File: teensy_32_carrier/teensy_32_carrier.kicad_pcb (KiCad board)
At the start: 4 copper layers, 65 x 56.5 mm, 65 parts, among them J1 CON_01X03_PTH_2.54MM, J10 CJ, J11 CJ, J12 CJ, J13 CJ, J14 CJ, J2 CON_01X08_PTH_2.54MM, J3 CON_01X06_PTH_2.54MM, J4 CON_01X04_PTH_2.54MM, J5 CON_01X03_PTH_2.54MM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

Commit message: start routing
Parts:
- moved D1 41.5 mm to (137.0, 68.5), turned to 0 degrees
- moved R4 37.8 mm to (136.5, 69.5), turned to 0 degrees
- moved R5 37.8 mm to (136.5, 68.0), turned to 0 degrees
- moved R3 34.0 mm to (133.0, 70.0), turned to 0 degrees
- moved R8 14.6 mm to (95.5, 108.5), turned to 270 degrees
- moved R12 2.24 mm to (84.0, 82.5)
- moved R11 2.22 mm to (81.5, 82.5)
- moved C6 1.50 mm to (93.0, 86.5)
- moved R9 1.12 mm to (105.5, 109.5), turned to 270 degrees
- moved R16 0.74 mm to (97.5, 96.0)
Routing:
- net GND: track 0.00 -> 145.1 mm, vias 0 -> 6
- net +5V: track 0.00 -> 65.5 mm, vias 0 -> 4
- net /Power/OFF_NODE: track 0.00 -> 29.6 mm, vias 0 -> 3
- net /Power/BAT_IN: track 0.00 -> 25.3 mm, vias 0 -> 1
- net /Power/VR_FB: track 0.00 -> 25.1 mm, vias 0 -> 2
- net +BATT: track 0.00 -> 21.9 mm, vias 0 -> 1
- net /Power/VR_SW: track 0.00 -> 18.1 mm, vias 0 -> 1
- net /Power/VR_BT: track 0.00 -> 16.7 mm, vias 0 -> 2
- net /Power/VR_VI: track 0.00 -> 14.8 mm, vias 0 -> 1
- net /Power/VR_EN: track 0.00 -> 6.13 mm, vias 0 -> 1
- net /Power/VR_SS: track 0.00 -> 5.48 mm, vias 0 -> 1
- net Net-(D1-Pad4): track 0.00 -> 4.01 mm, vias 0 -> 1
- net Net-(D1-Pad3): track 0.00 -> 3.14 mm, vias 0 -> 1
- net Net-(D1-Pad2): track 0.00 -> 3.10 mm, vias 0 -> 1
- net /Power/VR_RT: track 0.00 -> 2.19 mm, vias 0 -> 1
- added copper zone on B.Cu, net +5V
- added copper zone on F.Cu, net +5V
- added copper zone on F.Cu, net +BATT
- added copper zone on F.Cu, net /Power/BAT_IN
- added copper zone on F.Cu, net /Power/VR_SW
- added copper zone on B.Cu, net GND
- added copper zone on F.Cu, net GND

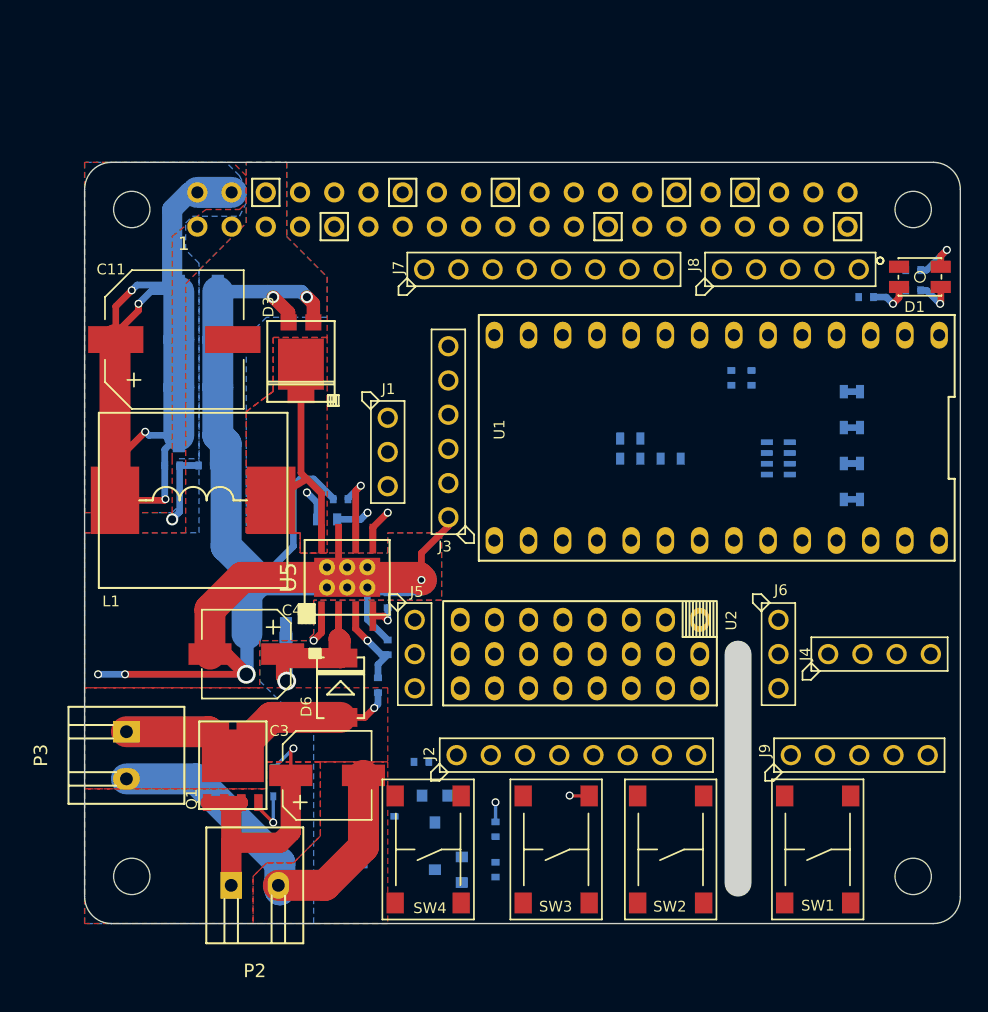
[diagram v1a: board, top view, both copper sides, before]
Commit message: routing getting closer to first completion
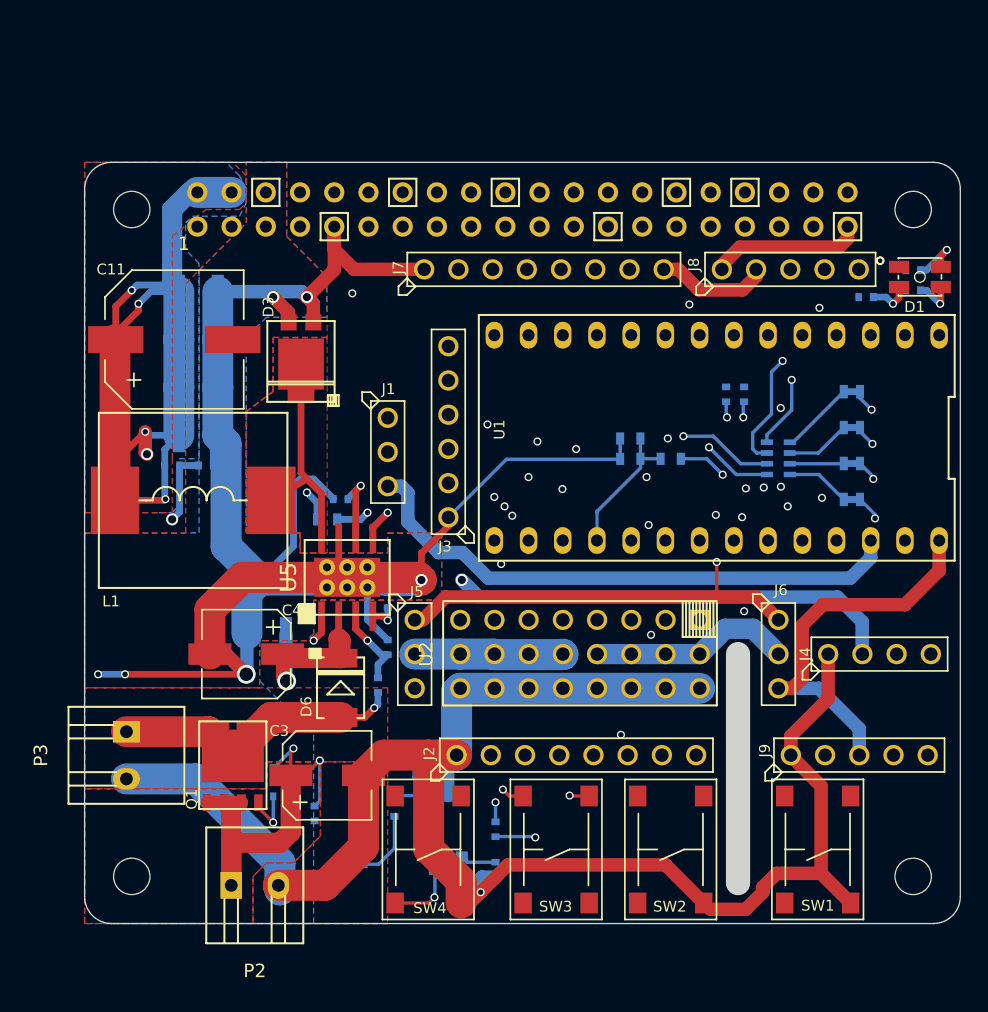
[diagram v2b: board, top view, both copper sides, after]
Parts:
- moved R8 3.43 mm to (92.1, 108.3)
- moved R14 1.33 mm to (124.0, 77.2)
- moved R13 1.27 mm to (122.6, 77.2)
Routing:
- net GND: track 145.1 -> 302.3 mm, vias 6 -> 7
- net +5VP: track 0.00 -> 93.0 mm, vias 0 -> 1
- net +5V: track 65.5 -> 155.5 mm, vias 4 -> 5
- net /Power/BAT_IN: track 25.3 -> 89.0 mm, vias 1 -> 3
- net /R_RXD: track 0.00 -> 56.2 mm, vias 0 -> 2
- net /R_TXD: track 0.00 -> 54.6 mm, vias 0 -> 1
- net /DIN: track 0.00 -> 46.6 mm, vias 0 -> 4
- net /DOUT: track 0.00 -> 45.5 mm, vias 0 -> 2
- net /Power/ON_NODE: track 0.00 -> 45.3 mm, vias 0 -> 2
- net +BATT: track 21.9 -> 64.1 mm, vias 1 -> 3
- net +3V3: track 0.00 -> 41.9 mm
- net /R_4: track 0.00 -> 41.7 mm, vias 0 -> 1
- net /D6: track 0.00 -> 41.2 mm, vias 0 -> 3
- net /Power/OFF_NODE: track 29.6 -> 70.8 mm
- net /D10: track 0.00 -> 38.8 mm, vias 0 -> 2
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
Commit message: version 0.1 ready to test upload
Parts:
- moved C3 0.70 mm to (93.0, 104.8)
- moved D6 0.45 mm to (93.8, 98.6)
- moved R11 0.20 mm to (81.5, 82.7)
- moved R12 0.20 mm to (84.0, 82.7)
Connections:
- P1 pad 11: /R_17 -> /Power/PRWON1
- P1 pad 37: /Power/PRWON1 -> /R_26
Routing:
- net GND: track 302.3 -> 390.7 mm, vias 7 -> 13
- net +5V: track 155.5 -> 243.4 mm, vias 5 -> 9
- net /Power/PWRON2: track 4.99 -> 86.7 mm, vias 0 -> 4
- net /R_19: track 0.00 -> 64.8 mm, vias 0 -> 4
- net +2V5: track 8.42 -> 71.6 mm, vias 0 -> 1
- net /R_13: track 0.00 -> 61.0 mm, vias 0 -> 4
- net /R_SDA: track 30.0 -> 81.3 mm
- net /Power/PRWON1: track 2.67 -> 53.0 mm, vias 0 -> 2
- net /R_SCL: track 36.7 -> 86.2 mm
- net +BATT: track 64.1 -> 83.9 mm, vias 3 -> 5
- net /R_20: track 0.00 -> 13.9 mm, vias 0 -> 1
- net /R_16: track 0.00 -> 13.8 mm, vias 0 -> 1
- net /R_21: track 0.00 -> 11.0 mm, vias 0 -> 1
- net /SDA: track 25.2 -> 33.4 mm
- net /SCL: track 26.5 -> 33.4 mm
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- added copper zone on F.Cu, net +2V5
- added copper zone on In1.Cu, net +5V
- added copper zone on In1.Cu, net +BATT
- added copper zone on In1.Cu, net GND
- added copper zone on In2.Cu, net GND
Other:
- net class Default: trace_width 0.25 -> 0.13; via_dia 0.6 -> 0.465; via_drill 0.4 -> 0.305
- board text added: "+"
- board text added: "+3"
- board text added: "+5"
- board text added: "+V"
- board text added: "-"
- board text added: "10"
- board text added: "13"
- board text added: "14"
- board text added: "15"
- board text added: "17"
- board text added: "20"
- board text added: "21"
- board text added: "22"
- board text added: "23"
- board text added: "25"
- board text added: "3"
- board text added: "3V"
- board text added: "4"
- board text added: "5"
- board text added: "5V/5A buck regulator"
- board text added: "6"
- board text added: "9"
- board text added: "Bat"
- board text added: "Bat In"
- board text added: "Bat Out"
- board text added: "C"
- board text added: "C0"
- board text added: "C1"
- board text added: "D"
- board text added: "DI"
- board text added: "DO"
- board text added: "G"
- board text added: "I2C"
- board text added: "MCU On"
- board text added: "MI"
- board text added: "MO"
- board text added: "Off"
- board text added: "On"
- board text added: "Pi 13"
- board text added: "Pi 19"
- board text added: "Pi I/O"
- board text added: "RX3"
- board text added: "Raspberry Pi Car Shield v 0.1"
- board text added: "Red"
- board text added: "SC"
- board text added: "SD"
- board text added: "SPI"
- board text added: "Separate Pi and Teensy"
- board text added: "Switched Out"
- board text added: "TX3"
- board text added: "T_2 or R_17 Hi/Lo Power On/Off"
- board text added: "Teesny 3.2 or Teensy 3 LC"
- board text added: "USB"
- board text added: "Vbat"
- board text added: "https://github.com/jwatte/donkey_racing"
- board text removed: "Stay On"

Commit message: prep for order v0.1
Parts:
- C12: value 311-2054-1-ND -> 311-3532-1-ND
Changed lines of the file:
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@@
   (page A4)
   (layers
-    (0 F.Cu signal)
-    (1 In1.Cu signal)
-    (2 In2.Cu signal)
-    (31 B.Cu signal)
+    (0 F.Cu signal hide)
+    (1 In1.Cu signal hide)
+    (2 In2.Cu signal hide)
+    (31 B.Cu signal hide)
     (32 B.Adhes user hide)
     (33 F.Adhes user hide)
@@
     (visible_elements FFFEC77F)
     (pcbplotparams
-      (layerselection 0x00030_80000001)
-      (usegerberextensions false)
+      (layerselection 0x010fc_80000007)
+      (usegerberextensions true)
       (excludeedgelayer true)
       (linewidth 0.100000)
@@
       (psa4output false)
       (plotreference true)
-      (plotvalue true)
+      (plotvalue false)
       (plotinvisibletext false)
       (padsonsilk false)
-      (subtractmaskfromsilk false)
+      (subtractmaskfromsilk true)
       (outputformat 1)
       (mirror false)
-      (drillshape 1)
+      (drillshape 0)
       (scaleselection 1)
-      (outputdirectory ""))
+      (outputdirectory macrofab_order_20170820/))
   )
   (net 0 "")
@@
       (effects (font (size 0.8 0.8) (thickness 0.15)) (justify mirror))
     )
-    (fp_text value 311-2054-1-ND (at 0.33782 3.83032 180) (layer B.Fab)
-      (effects (font (size 0.8 0.8) (thickness 0.15)) (justify mirror))
-    )
+    (fp_text value 311-3532-1-ND (at 0.33782 3.83032 180) (layer B.Fab)
+      (effects (font (size 0.8 0.8) (thickness 0.15)) (justify mirror))
+    )

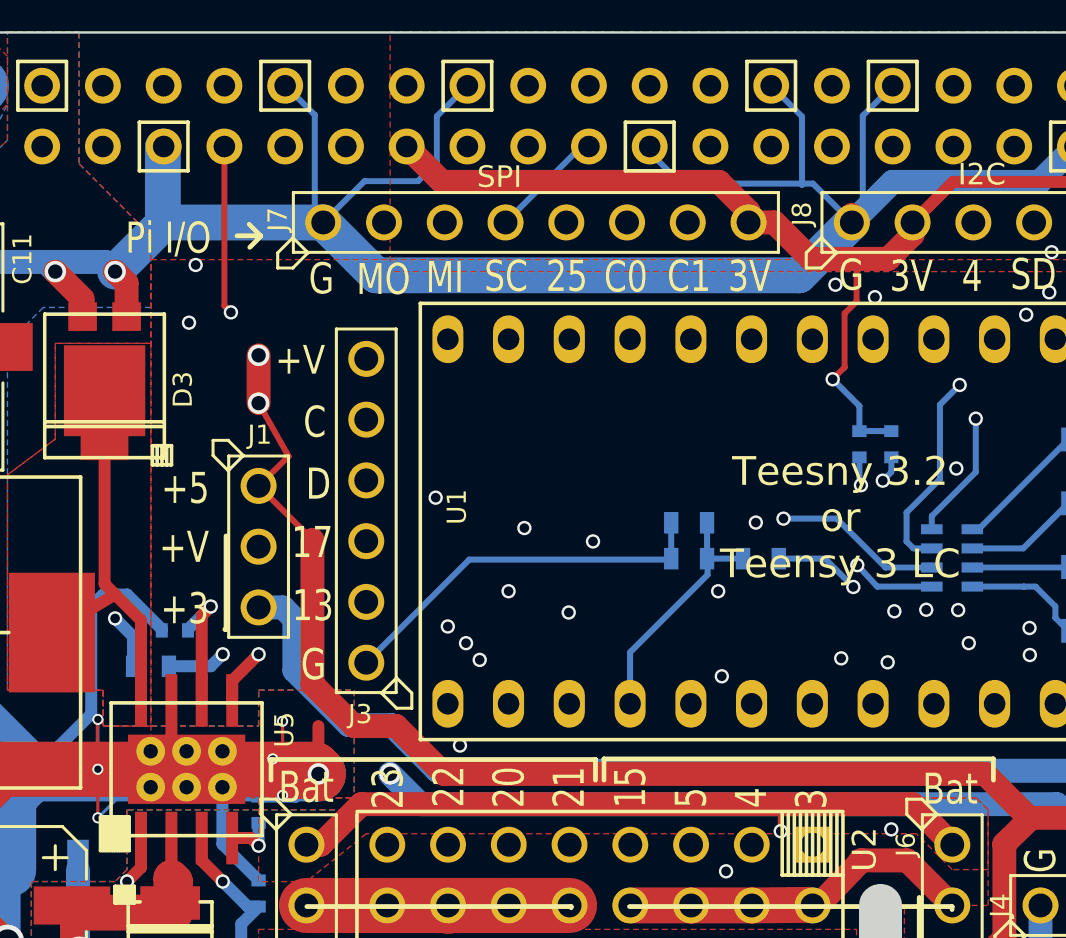
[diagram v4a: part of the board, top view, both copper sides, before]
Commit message: trying to fit an RTC and the Hat EEPROM, but no.
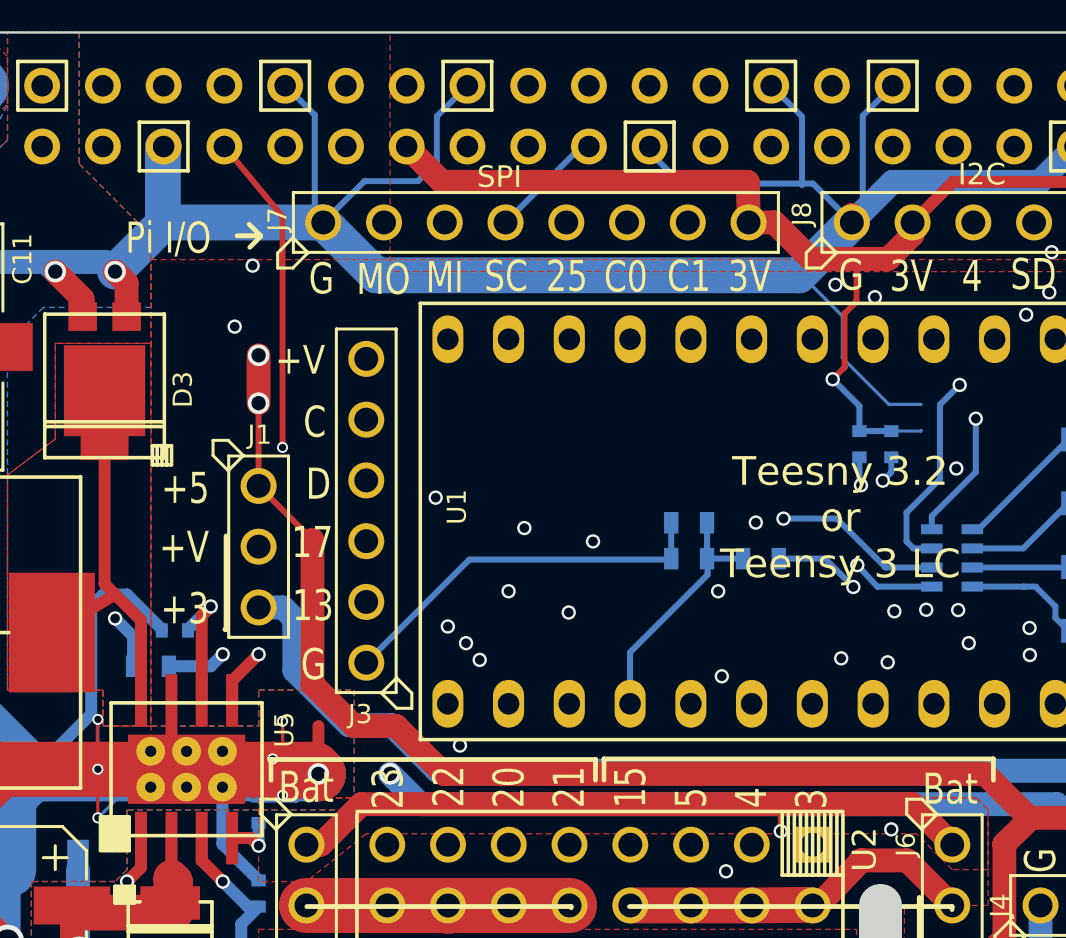
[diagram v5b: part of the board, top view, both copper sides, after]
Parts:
- J1, J5, J6: value CON_01X03_PTH_2.54MM -> MF-CON-2.54mm-01x03
- J2, J7: value CON_01X08_PTH_2.54MM -> MF-CON-2.54mm-01x08
- J3: value CON_01X06_PTH_2.54MM -> MF-CON-2.54mm-01x06
- J4: value CON_01X04_PTH_2.54MM -> MF-CON-2.54mm-01x04
- J8, J9: value CON_01X05_PTH_2.54MM -> MF-CON-2.54mm-01x05
- R11, R15: value MF-RES-0402-100K -> 311-100KLRCT-ND
- R17, R6, R7: value MF-RES-0402-10K -> MF-RES-0402-18K
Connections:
- net /Power/PRWON1 renamed /R_17
- net /Power/PWRON2 renamed /PWRON
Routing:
- net GND: track 390.7 -> 402.1 mm
- net /R_SCL: track 86.2 -> 90.0 mm
- net /R_17: track 53.0 -> 55.9 mm
- net +2V5: track 71.6 -> 73.5 mm
- net /R_SDA: track 81.3 -> 83.0 mm
- net +5V: track 243.4 -> 242.6 mm
- net /PWRON: track 86.7 -> 86.1 mm
- net /R_ID_SC: track 0.00 -> 0.51 mm

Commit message: version 2 macrofab project
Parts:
- added C13: MF-CAP-0402-0.1uF, MF_Passives:MF_Passives-C0402, B.Cu at (121.6, 57.1)
- added C14: MF-CAP-0402-0.1uF, MF_Passives:MF_Passives-C0402, B.Cu at (87.0, 58.7)
- added C15: MF-CAP-0402-8.2pF, MF_Passives:MF_Passives-C0402, B.Cu at (87.0, 52.1)
- added C2: KR-5R5V334-R, Capacitors_THT:C_Rect_L7.2mm_W11.0mm_P5.00mm_FKS2_FKP2_MKS2_MKP2, F.Cu at (84.2, 57.5)
- added D4: MF-DIO-SOD123-BAT42, MF_Discrete_Semiconductor:MF_Discrete_Semiconductor-SOD-123, B.Cu at (78.5, 55.5)
- added J15: CJ, teensy:CJ-2, B.Cu at (117.3, 52.2)
- added J16: CON_01X04_PTH_2.54MM, MF_Connectors:MF_Connectors-PTH_2.54MM_01X04, F.Cu at (101.0, 52.0)
- added R18: MF-RES-0402-2K, MF_Passives:MF_Passives-R0402, B.Cu at (118.8, 57.1)
- added R19: MF-RES-0402-2K, MF_Passives:MF_Passives-R0402, B.Cu at (120.2, 57.0)
- added R20: MF-RES-0402-10K, MF_Passives:MF_Passives-R0402, B.Cu at (123.0, 53.6)
- added R21: MF-RES-0402-470, MF_Passives:MF_Passives-R0402, B.Cu at (81.5, 55.1)
- added U6: PCF8563, teensy:TSSOP-8, B.Cu at (89.9, 56.4)
- added U7: M24C32-5, teensy:UFDFPN5, B.Cu at (120.8, 54.3)
- added Y1: Crystal, teensy:SC-20S, B.Cu at (89.7, 52.0)
- moved J7 11.7 mm to (104.8, 57.0)
- moved J8 11.1 mm to (129.0, 57.0)
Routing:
- net +2V5: track 73.5 -> 111.1 mm, vias 1 -> 3
- net GND: track 402.1 -> 439.4 mm, vias 13 -> 14
- net +5V: track 242.6 -> 276.3 mm
- net /R_ID_SD: track 0.00 -> 16.3 mm, vias 0 -> 1
- net /R_SDA: track 83.0 -> 97.2 mm, vias 3 -> 5
- net Net-(J15-Pad1): track 0.00 -> 12.7 mm, vias 0 -> 2
- net /R_ID_SC: track 0.51 -> 12.1 mm, vias 0 -> 1
- net /R_SCK: track 4.80 -> 15.0 mm
- net Net-(C14-Pad1): track 0.00 -> 8.66 mm
- net /R_MOSI: track 4.80 -> 13.4 mm
- net /R_MISO: track 4.80 -> 13.1 mm
- net /R_4: track 40.9 -> 47.3 mm, vias 1 -> 0
- net /R_SCL: track 90.0 -> 94.7 mm, vias 2 -> 6
- net Net-(C15-Pad1): track 0.00 -> 3.72 mm
- net Net-(D4-PadCATH): track 0.00 -> 3.18 mm
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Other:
- board size 65 x 56.5 mm -> 65 x 66.5 mm
- board text added: "2017-09-14"
- board text added: "3.3V"
- board text added: "5V"
- board text added: "CE0"
- board text added: "CE`1"
- board text added: "~WRPROT"
- board text removed: "3V"
- board text removed: "C0"
- board text removed: "C1"
- board text removed: "Pi I/O"
- board text removed: "SD"
